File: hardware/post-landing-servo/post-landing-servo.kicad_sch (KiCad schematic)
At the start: 5 parts, among them J1 Conn_01x06, J2 DE9_Pins, J3 DE9_Pins

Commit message: Gavin and Remco pcb to be checked
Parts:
- removed J1: Conn_01x06, symbol Connector_Generic:Conn_01x06
- added H1, H2: MountingHole_Pad, MountingHole:MountingHole_3.2mm_M3_Pad_Via, symbol Mechanical:MountingHole_Pad
- added J1, J4: Conn_01x08, Custom:ZH-6PWB_knockoff, symbol Connector_Generic:Conn_01x08
- added J5: Conn_01x06, Connector_JST:JST_EH_B6B-EH-A_1x06_P2.50mm_Vertical, symbol Connector_Generic:Conn_01x06
- JP1, JP2: footprint (none) -> Jumper:SolderJumper-2_P1.3mm_Bridged_Pad1.0x1.5mm
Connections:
- net +24V: now also J1.1 (Pin_1), J1.2 (Pin_2), J4.1 (Pin_1), J4.2 (Pin_2), J5.2 (Pin_2)
- net +5V: now also J5.1 (Pin_1)
- net GND: now also H1.1, H2.1, J1.3 (Pin_3), J1.4 (Pin_4), J1.7 (Pin_7), J1.8 (Pin_8), J4.3 (Pin_3), J4.4 (Pin_4), J4.7 (Pin_7), J4.8 (Pin_8), J5.3 (Pin_3), J5.4 (Pin_4)
- net CAN_A_H renamed CAN_A+
- net CAN_A+: now also J1.6 (Pin_6), J4.6 (Pin_6)
- net CAN_A_L renamed CAN_A-
- net CAN_A-: now also J1.5 (Pin_5), J4.5 (Pin_5)
- net CAN_B_H renamed CAN_B+
- net CAN_B_L renamed CAN_B-
- new net SIG1: J5.5 (Pin_5)
- new net SIG2: J5.6 (Pin_6)
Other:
- note added: "HEADER_PINS"
- note added: "MOUNTING_HOLE"

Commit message: feat: Added GND vias to servo pcb
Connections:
- net SIGNAL is gone; now on net SIG1: J2.5, J3.5
- net SIG2: now also J2.6, J3.6
- no-connect marks 2 -> 0
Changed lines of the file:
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@@
+	)
+	(junction
+		(at 242.57 57.15)
+		(diameter 0)
+		(color 0 0 0 0)
 	)
 	(junction
@@
 	)
 	(junction
+		(at 237.49 54.61)
+		(diameter 0)
+		(color 0 0 0 0)
+	)
+	(junction
 		(at 217.17 41.91)
 		(diameter 0)
@@
 		(color 0 0 0 0)
 	)
-	(no_connect
-		(at 259.08 69.85)
-	)
-	(no_connect
-		(at 259.08 36.83)
+	(junction
+		(at 247.65 62.23)
+		(diameter 0)
+		(color 0 0 0 0)
 	)
 	(wire
@@
 		)
 	)
-	(label "SIGNAL"
-		(at 259.08 52.07 180)
+	(label "SIG2"
+		(at 259.08 69.85 180)
 		(effects
 			(font
@@
 		)
 	)
+	(label "SIG1"
+		(at 259.08 52.07 180)
+		(effects
+			(font
+				(size 1.27 1.27)
+			)
+			(justify right bottom)
+		)
+	)
 	(label "SIG2"
 		(at 194.31 49.53 180)
@@
 		)
 	)
+	(label "SIG2"
+		(at 259.08 36.83 180)
+		(effects
+			(font
+				(size 1.27 1.27)
+			)
+			(justify right bottom)
+		)
+	)
 	(label "SIG1"
 		(at 194.31 46.99 180)
@@
 		)
 	)
-	(label "SIGNAL"
+	(label "SIG1"
 		(at 259.08 19.05 180)
 		(effects
@@
 	)
 	(symbol
+		(lib_id "power:PWR_FLAG")
+		(at 242.57 57.15 0)
+		(unit 1)
+		(exclude_from_sim no)
+		(in_bom yes)
+		(on_board yes)
+		(dnp no)
+		(property "Reference" "#FLG02"
+			(at 242.57 55.245 0)
+			(effects
+				(font
+					(size 1.27 1.27)
+				)
+				(hide yes)
+			)
+		)
+		(property "Value" "PWR_FLAG"
+			(at 248.666 55.88 0)
+			(effects
+				(font
+					(size 1.27 1.27)
+				)
+			)
+		)
+		(property "Footprint" ""
+			(at 242.57 57.15 0)
+			(effects
+				(font
+					(size 1.27 1.27)
+				)
+				(hide yes)
+			)
+		)
+		(property "Datasheet" "~"
+			(at 242.57 57.15 0)
+			(effects
+				(font
+					(size 1.27 1.27)
+				)
+				(hide yes)
+			)
+		)
+		(property "Description" "Special symbol for telling ERC where power comes from"
+			(at 242.57 57.15 0)
+			(effects
+				(font
+					(size 1.27 1.27)
+				)
+				(hide yes)
+			)
+		)
+		(pin "1"
+		)
+		(instances
+			(project ""
+				(path "/27b9b8c2-577d-47b7-89a1-ebeb4244826d"
+					(reference "#FLG02")
+					(unit 1)
+				)
+			)
+		)
+	)
+	(symbol
+		(lib_id "power:PWR_FLAG")
+		(at 237.49 54.61 0)
+		(unit 1)
+		(exclude_from_sim no)
+		(in_bom yes)
+		(on_board yes)
+		(dnp no)
+		(fields_autoplaced yes)
+		(property "Reference" "#FLG01"
+			(at 237.49 52.705 0)
+			(effects
+				(font
+					(size 1.27 1.27)
+				)
+				(hide yes)
+			)
+		)
+		(property "Value" "PWR_FLAG"
+			(at 237.49 49.53 0)
+			(effects
+				(font
+					(size 1.27 1.27)
+				)
+			)
+		)
+		(property "Footprint" ""
+			(at 237.49 54.61 0)
+			(effects
+				(font
+					(size 1.27 1.27)
+				)
+				(hide yes)
+			)
+		)
+		(property "Datasheet" "~"
+			(at 237.49 54.61 0)
+			(effects
+				(font
+					(size 1.27 1.27)
+				)
+				(hide yes)
+			)
+		)
+		(property "Description" "Special symbol for telling ERC where power comes from"
+			(at 237.49 54.61 0)
+			(effects
+				(font
+					(size 1.27 1.27)
+				)
+				(hide yes)
+			)
+		)
+		(pin "1"
+		)
+		(instances
+			(project ""
+				(path "/27b9b8c2-577d-47b7-89a1-ebeb4244826d"
+					(reference "#FLG01")
+					(unit 1)
+				)
+			)
+		)
+	)
+	(symbol
 		(lib_id "power:+24V")
 		(at 242.57 29.21 180)
@@
 					(unit 1)
 				)
+			)
+		)
+	)
+	(symbol
+		(lib_id "power:PWR_FLAG")
+		(at 247.65 62.23 0)
+		(unit 1)
+		(exclude_from_sim no)
+		(in_bom yes)
+		(on_board yes)
+		(dnp no)
+		(property "Reference" "#FLG03"
+			(at 247.65 60.325 0)
+			(effects
+				(font
+					(size 1.27 1.27)
+				)
+				(hide yes)
+			)
+		)
+		(property "Value" "PWR_FLAG"
+			(at 253.746 60.96 0)
+			(effects
+				(font
+					(size 1.27 1.27)
+				)
+			)
+		)
+		(property "Footprint" ""
+			(at 247.65 62.23 0)
+			(effects
+				(font
+					(size 1.27 1.27)
+				)
+				(hide yes)
+			)
+		)
+		(property "Datasheet" "~"
+			(at 247.65 62.23 0)
+			(effects
+				(font
+					(size 1.27 1.27)
+				)
+				(hide yes)
+			)
+		)
+		(property "Description" "Special symbol for telling ERC where power comes from"
+			(at 247.65 62.23 0)
+			(effects
+				(font
+					(size 1.27 1.27)
+				)
+				(hide yes)
+			)
+		)
+		(pin "1"
+		)
+		(instances
+			(project "post-landing-servo"
+				(path "/27b9b8c2-577d-47b7-89a1-ebeb4244826d"
+					(reference "#FLG03")
+					(unit 1)
+				)

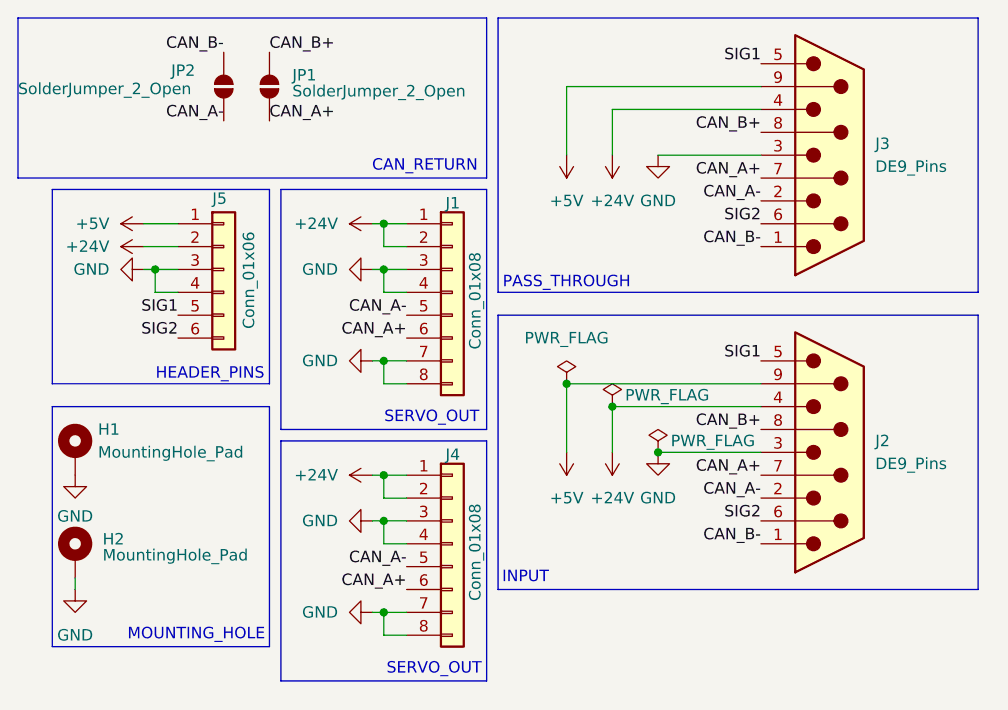
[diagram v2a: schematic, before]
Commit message: fix: Changed DE-9 headers to female
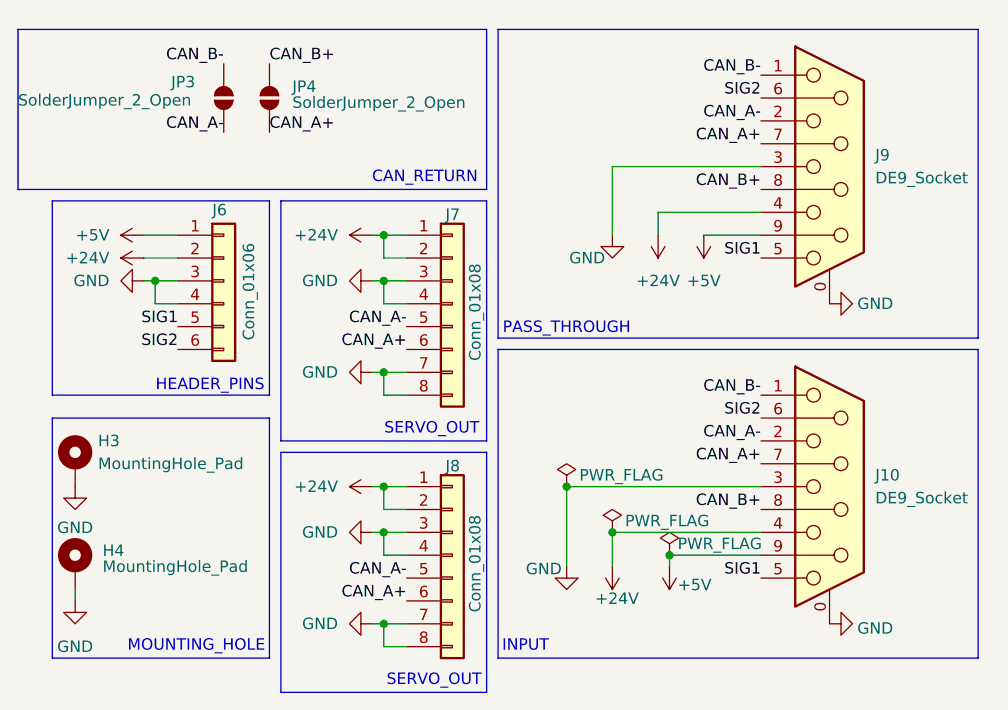
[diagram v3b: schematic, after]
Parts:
- removed H1, H2: MountingHole_Pad, MountingHole:MountingHole_3.2mm_M3_Pad_Via, symbol Mechanical:MountingHole_Pad
- removed J1, J4: Conn_01x08, Custom:ZH-6PWB_knockoff, symbol Connector_Generic:Conn_01x08
- removed J2, J3: DE9_Pins, Connector_Dsub:DSUB-9_Pins_Horizontal_P2.77x2.84mm_EdgePinOffset4.94mm_Housed_MountingHolesOffset4.94mm, symbol Connector:DE9_Pins
- removed J5: Conn_01x06, Connector_JST:JST_EH_B6B-EH-A_1x06_P2.50mm_Vertical, symbol Connector_Generic:Conn_01x06
- removed JP1, JP2: SolderJumper_2_Open, Jumper:SolderJumper-2_P1.3mm_Bridged_Pad1.0x1.5mm, symbol Jumper:SolderJumper_2_Open
- added H3, H4: MountingHole_Pad, MountingHole:MountingHole_3.2mm_M3_Pad_Via, symbol Mechanical:MountingHole_Pad
- added J10, J9: DE9_Socket, Connector_Dsub:DSUB-9_Socket_Horizontal_P2.77x2.84mm_EdgePinOffset4.94mm_Housed_MountingHolesOffset4.94mm, symbol Connector:DE9_Socket_MountingHoles
- added J6: Conn_01x06, Connector_JST:JST_EH_B6B-EH-A_1x06_P2.50mm_Vertical, symbol Connector_Generic:Conn_01x06
- added J7, J8: Conn_01x08, Custom:ZH-6PWB_knockoff, symbol Connector_Generic:Conn_01x08
- added JP3, JP4: SolderJumper_2_Open, Jumper:SolderJumper-2_P1.3mm_Open_Pad1.0x1.5mm, symbol Jumper:SolderJumper_2_Open
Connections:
- net +24V: now also J10.4, J6.2 (Pin_2), J7.1 (Pin_1), J7.2 (Pin_2), J8.1 (Pin_1), J8.2 (Pin_2), J9.4
- net +5V: now also J10.9, J6.1 (Pin_1), J9.9
- net CAN_A+: now also J10.7, J7.6 (Pin_6), J8.6 (Pin_6), J9.7, JP4.1 (A)
- net CAN_A-: now also J10.2, J7.5 (Pin_5), J8.5 (Pin_5), J9.2, JP3.1 (A)
- net CAN_B+: now also J10.8, J9.8, JP4.2 (B)
- net CAN_B-: now also J10.1, J9.1, JP3.2 (B)
- net GND: now also H3.1, H4.1, J10.0 (PAD), J10.3, J6.3 (Pin_3), J6.4 (Pin_4), J7.3 (Pin_3), J7.4 (Pin_4), J7.7 (Pin_7), J7.8 (Pin_8), J8.3 (Pin_3), J8.4 (Pin_4), J8.7 (Pin_7), J8.8 (Pin_8), J9.0 (PAD), J9.3
- net SIG1: now also J10.5, J6.5 (Pin_5), J9.5
- net SIG2: now also J10.6, J6.6 (Pin_6), J9.6

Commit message: Feat: Reroute and minor fixes
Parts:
- removed J7, J8: Conn_01x08, Custom:ZH-6PWB_knockoff, symbol Connector_Generic:Conn_01x08
- added J1, J2: Conn_01x06, Connector_JST:JST_ZH_B6B-ZR-SM4-TF_1x06-1MP_P1.50mm_Vertical, symbol Connector_Generic:Conn_01x06
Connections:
- net +24V: now also J1.1 (Pin_1), J1.2 (Pin_2), J2.1 (Pin_1), J2.2 (Pin_2)
- net CAN_A+: now also J1.6 (Pin_6), J2.6 (Pin_6)
- net CAN_A-: now also J1.5 (Pin_5), J2.5 (Pin_5)
- net GND: now also J1.3 (Pin_3), J1.4 (Pin_4), J2.3 (Pin_3), J2.4 (Pin_4)
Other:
- moved on the sheet: H3, H4
